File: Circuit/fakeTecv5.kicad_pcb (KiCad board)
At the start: 2 copper layers, 25.4 x 52.1 mm, 78 parts, among them J1 EXTRA, J11 FET1 3,3, J12 FET2 3,3, J13 FET3 3,3, J14 GPS Pins, J16 Encoder Pads, J37 SCL, J38 JST-SH-4, J39 SDA, J40 3.3V, J41 GND, J42 FET1, J43 FET2, J44 FET3, J45 GND, J46 3.3V, J47 GND, J48 GND, J49 GND, J5 I2C Oled screen, J50 3.3V, J51 GND, J52 GND, J6 FET1 Drain, J7 FET2 Drain, J8 FET3 Drain, J9 JST-PH-2, Q1 AO3400A, Q2 AO3400A, Q3 AO3400A, SW1 Reset, SW2 SW_Push, U1 XB8089D0, U2 HT-RA62, U3 nice!nano v2

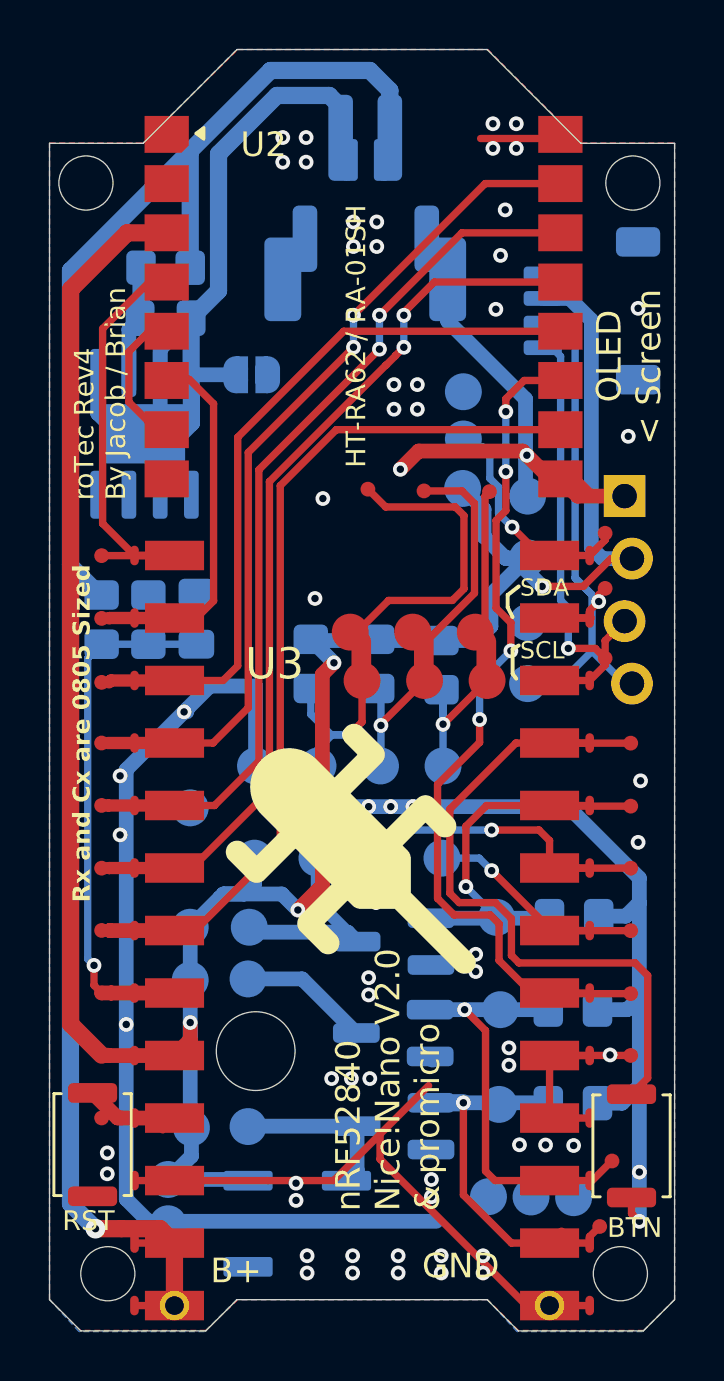
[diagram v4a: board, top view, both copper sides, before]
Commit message: hw: Battery connector clarification
Heltec LoRa32 is using Molex Picoblade... not JST
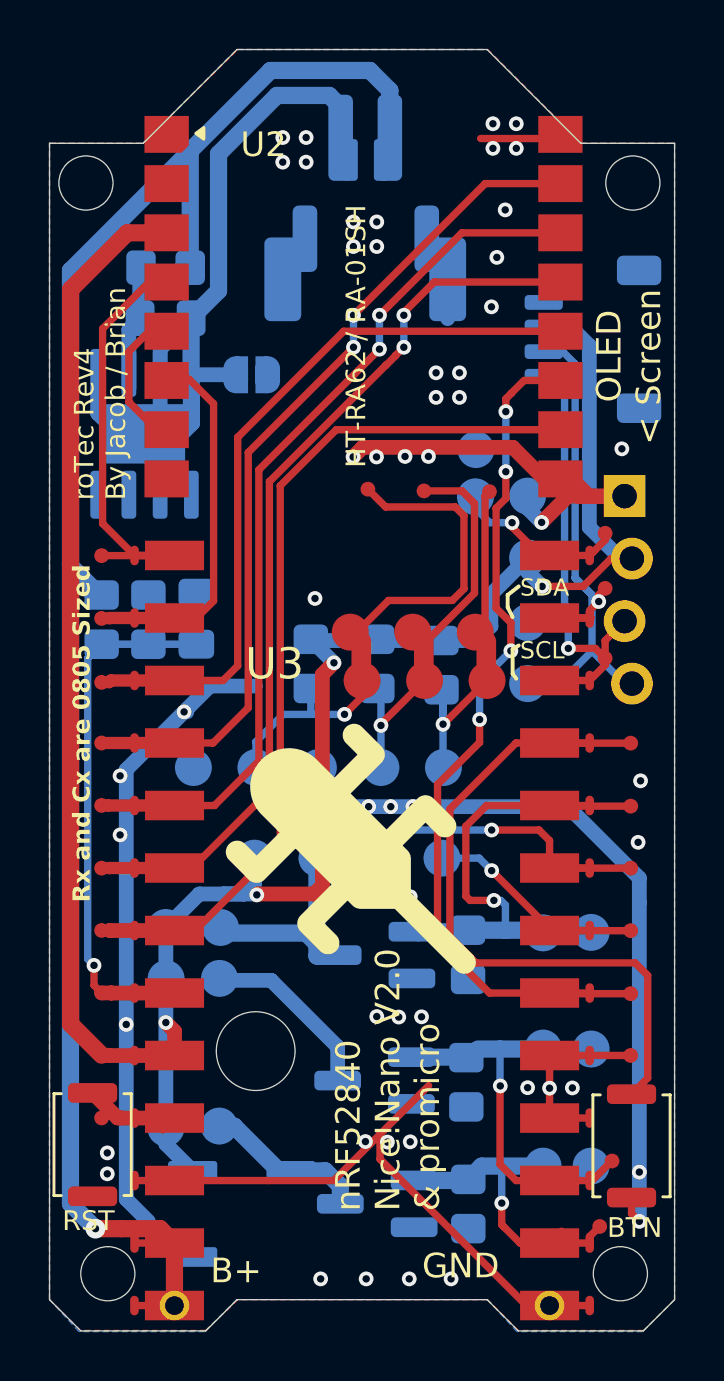
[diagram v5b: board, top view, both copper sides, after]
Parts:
- removed J46, J50: 3.3V, faketec:SMD_PAD_1x01
- removed J51, J52: GND, faketec:SMD_PAD_1x01
- J16: footprint faketec:SMD_PAD_1x04 -> faketec:SMD_PAD_1x05
- J9: value JST-PH-2 -> Molex PicoBlade 0532610271
- moved J49 10.8 mm to (120.9, 62.9)
- moved J48 7.31 mm to (120.9, 67.6)
- moved R3 5.90 mm to (115.9, 73.9), turned to 90 degrees
- moved R2 5.24 mm to (115.8, 69.0), turned to 90 degrees
- moved R1 4.59 mm to (115.9, 63.8), turned to 90 degrees
- moved Q3 3.23 mm to (112.2, 73.9)
- moved J44 3.08 mm to (118.9, 72.4)
- moved J47 2.74 mm to (120.9, 72.4)
- moved J16 2.52 mm to (104.7, 56.2)
- moved J45 2.40 mm to (116.2, 43.2)
- moved J1 2.40 mm to (116.2, 45.2)
- moved J43 2.34 mm to (118.9, 67.6)
- moved BZ1 2.29 mm to (106.7, 74.3)
- moved Q2 2.07 mm to (112.1, 68.9)
- moved J42 1.99 mm to (118.9, 62.9)
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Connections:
- J16 pad 3: /ENC_B -> GND
- J16 pad 4: /ENC_A -> /ENC_B
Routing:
- net GND: track 133.1 -> 108.4 mm, vias 67 -> 56
- net +3.3V: track 111.6 -> 100.8 mm
- net /FET3: track 16.3 -> 12.2 mm
- net /FET2: track 15.6 -> 12.5 mm
- net /EXTRA: track 7.40 -> 5.24 mm
- net /FET1: track 16.1 -> 18.1 mm
- net /GPS_GND: track 8.61 -> 10.6 mm
- net /VIBRATION: track 5.31 -> 7.30 mm
- net /SCL: track 19.4 -> 18.0 mm
- net /SDA: track 25.3 -> 24.1 mm
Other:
- board text added: "(EC11)"
- board text added: "5020 Buzzer >"
- board text added: "Direct GPIO Access"
- board text added: "P0.06( 6)"
- board text added: "P0.08( 8)"
- board text added: "P0.24(24)"
- board text added: "Qwiic"
- board text removed: "5020> Buzzer"
- board text removed: "<GND"
- board text removed: "P0.06 ( 6)"
- board text removed: "P0.08 ( 8)"
- board text removed: "P0.24 (24)"

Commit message: hw: Update schematic and connector to clarify battery connector
Including some photos and directions on locating the correct parts
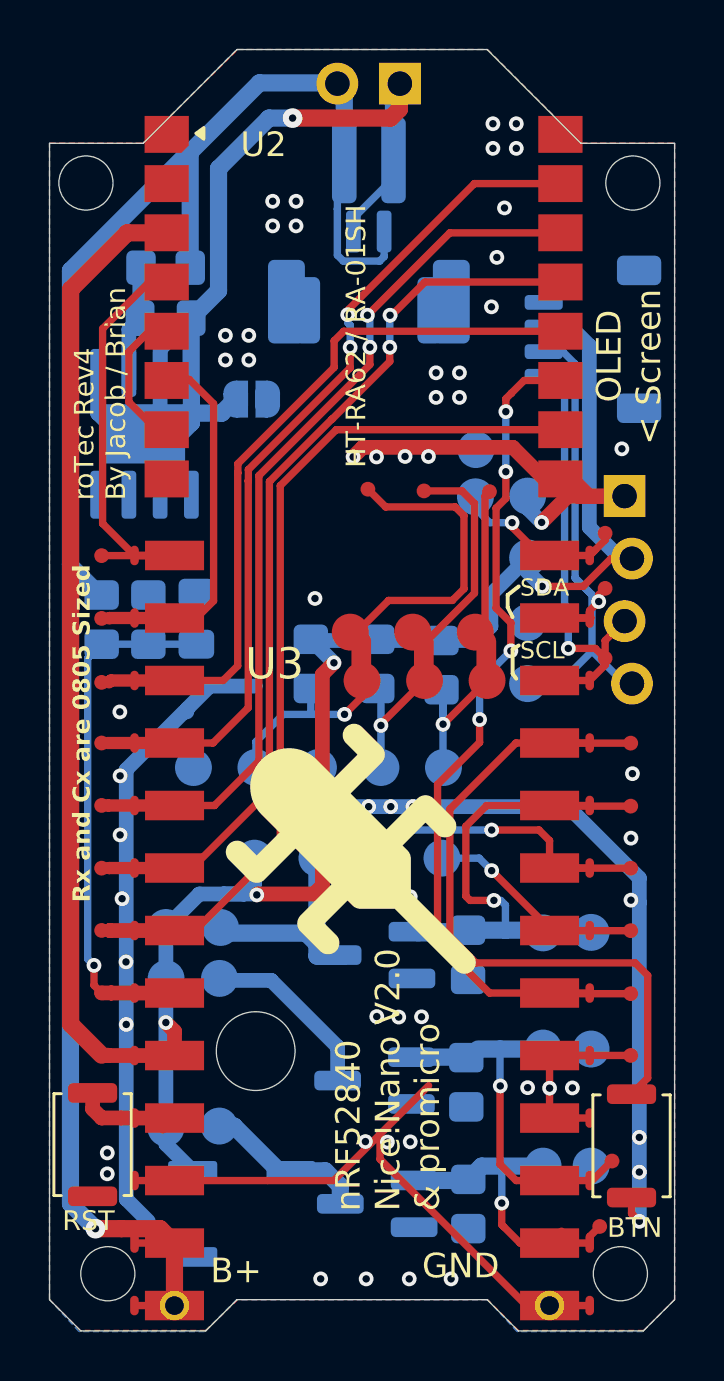
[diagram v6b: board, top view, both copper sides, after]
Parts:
- added J46: Conn_01x02_Socket, faketec:wirebond battery header, F.Cu at (113.1, 28.4)
- J9: footprint faketec:JST_PH_S2B-PH-SM4-TB_1x02-1MP_P2.00mm_Horizontal -> faketec:Combined_Battery_Connector_Molex_PicoBlade_P1.00_And_JST_PH_2.00mm
- moved JP1 0.99 mm to (107.1, 41.2)
- moved J9 0.92 mm to (111.9, 34.3)
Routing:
- net -BATT: track 32.9 -> 41.5 mm, vias 0 -> 1
- net GND: track 108.4 -> 103.7 mm, vias 56 -> 60
- net +BATT: track 72.7 -> 76.8 mm

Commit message: hw: Text Variable. Also mark as Rev5.
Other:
- board text added: "roTec Rev${REVISION} By Jacob / Brian"
- board text removed: "roTec Rev4 By Jacob / Brian"
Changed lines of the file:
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@@
 		)
 	)
+	(property "REVISION" "5")
 	(net 0 "")
 	(net 1 "/Batt%")
@@
 		(sheetname "/")
 		(sheetfile "fakeTecv5.kicad_sch")
-		(attr smd)
+		(attr smd exclude_from_bom)
 		(fp_text user "${REFERENCE}"
 			(at 0 -2.5 180)
@@
 			)
 		)
-		(property "Datasheet" "https://www.jst-mfg.com/product/pdf/eng/ePH.pdf"
+		(property "Datasheet" "https://www.molex.com/content/dam/molex/molex-dot-com/products/automated/en-us/salesdrawingpdf/532/53261/532610271_sd.pdf?inline"
 			(at 0 0 0)
 			(layer "B.Fab")
@@
 			)
 		)
-		(property "Description" "Combined footprint for JST_PH_S2B-PH-SM4-TB and JST_GH_SM02B-GHS-TB"
+		(property "Description" "1.25mm Pitch, PicoBlade PCB Header, Single Row, Right-Angle, Surface Mount, Tin (Sn) Plating, Friction Lock, 2 Circuits, Natural, Tape and Reel"
 			(at 0 0 0)
 			(layer "B.Fab")
@@
 		(layer "B.Mask")
 	)
-	(gr_line
-		(start 117.7 51.35)
-		(end 117.7 52.35)
-		(stroke
-			(width 0.16)
-			(type default)
-		)
-		(layer "F.SilkS")
-	)
-	(gr_line
-		(start 117.5 49.15)
-		(end 117.5 49.65)
-		(stroke
-			(width 0.16)
-			(type default)
-		)
-		(layer "F.SilkS")
-	)
 	(gr_poly
 		(pts
@@
 	)
 	(gr_line
-		(start 117.7 52.35)
-		(end 117.85 52.55)
-		(stroke
-			(width 0.16)
-			(type default)
-		)
-		(layer "F.SilkS")
-	)
-	(gr_line
-		(start 117.5 49.65)
-		(end 117.7 50.05)
-		(stroke
-			(width 0.16)
-			(type default)
-		)
-		(layer "F.SilkS")
-	)
-	(gr_line
-		(start 117.7 51.35)
-		(end 117.95 51.2)
-		(stroke
-			(width 0.16)
-			(type default)
-		)
-		(layer "F.SilkS")
-	)
-	(gr_line
-		(start 117.95 48.8)
-		(end 117.5 49.15)
-		(stroke
-			(width 0.16)
-			(type default)
-		)
-		(layer "F.SilkS")
-	)
-	(gr_line
 		(start 118.81 60.89)
 		(end 118.81 61.43)
@@
 		)
 	)
-	(gr_text "SDA"
-		(at 118 48.85 0)
-		(layer "F.SilkS")
-		(effects
-			(font
-				(size 0.7 0.7)
-				(thickness 0.16)
-			)
-			(justify left)
-		)
-	)
 	(gr_text "nRF52840\nNice!Nano V2.0\n& promicro"
 		(at 114.83 74.19 90)
@@
 		)
 	)
-	(gr_text "roTec Rev4\nBy Jacob / Brian"
+	(gr_text "roTec Rev${REVISION}\nBy Jacob / Brian"
 		(at 102.05 45.3 90)
 		(layer "F.SilkS" knockout)
@@
 		)
 	)
-	(gr_text "SCL"
-		(at 118 51.4 0)
-		(layer "F.SilkS")
-		(effects
-			(font
-				(size 0.7 0.7)
-				(thickness 0.16)
-			)
-			(justify left)
-		)
-	)

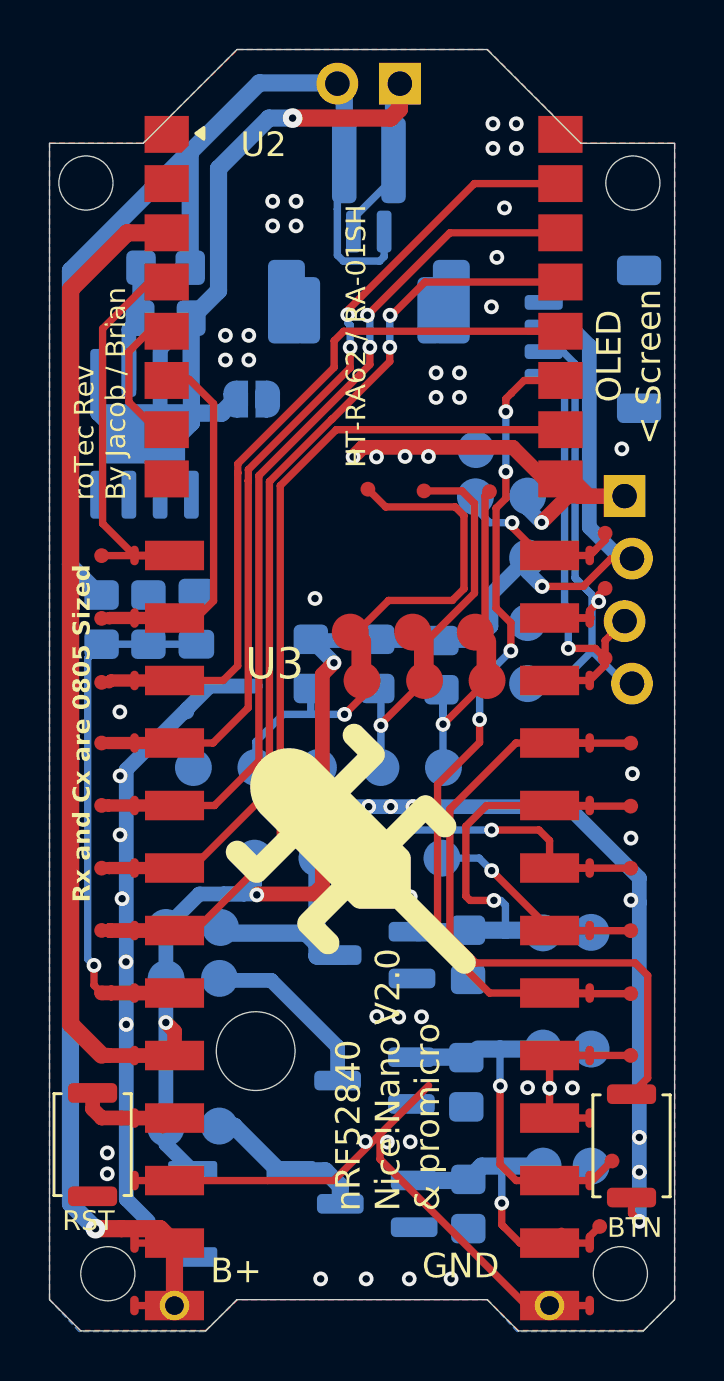
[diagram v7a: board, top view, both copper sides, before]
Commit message: hw: Add JST-SH-4 for encoder. Marked as Rev5.1
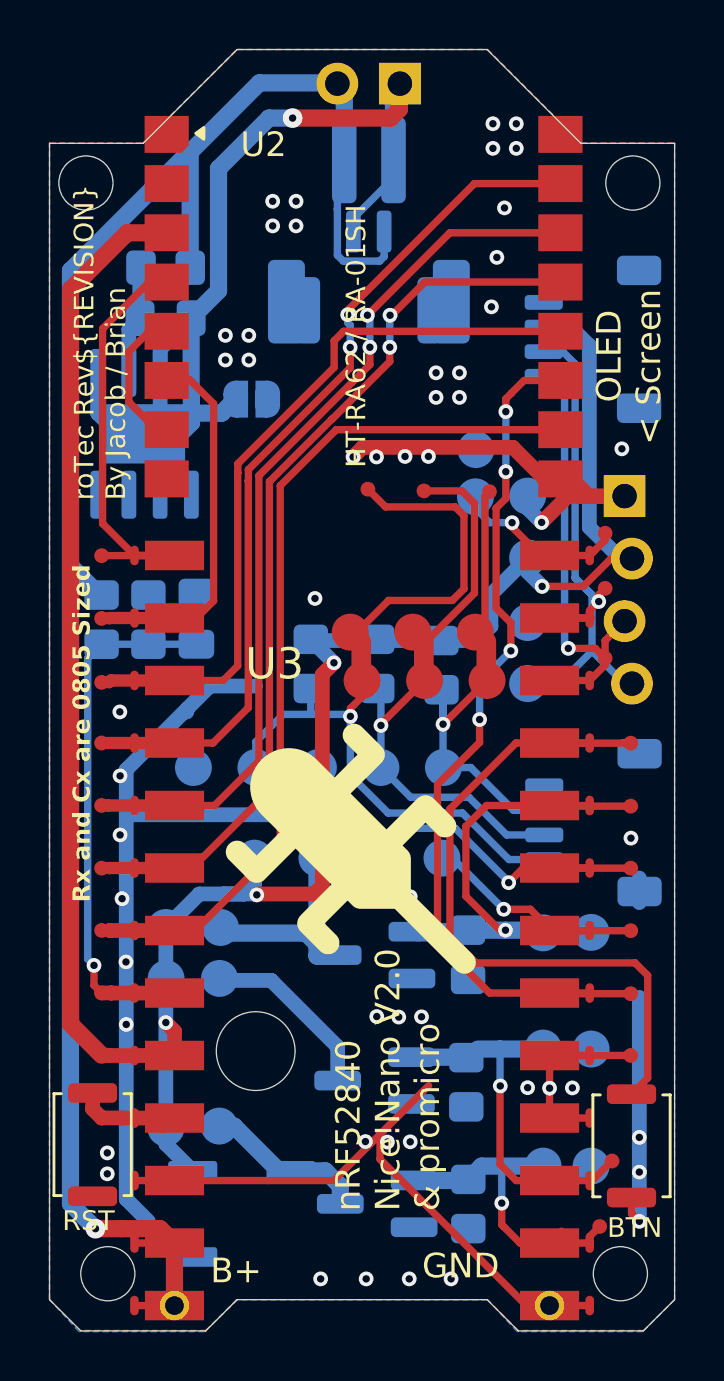
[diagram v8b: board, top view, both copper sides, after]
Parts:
- added J50: JST-SH-4, Connector_JST:JST_SH_SM04B-SRSS-TB_1x04-1MP_P1.00mm_Horizontal, B.Cu at (121.0, 58.4)
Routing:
- net /ENC_PUSH: track 21.1 -> 33.2 mm
- net GND: track 103.7 -> 93.8 mm, vias 60 -> 55
- net /ENC_B: track 15.1 -> 22.9 mm
- net /ENC_A: track 13.4 -> 18.2 mm
- net /FET1: track 18.1 -> 17.5 mm
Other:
- board text added: "ENC"
- board text added: "JST-SH-4"
- board text added: "SEL"
- board text removed: "Direct GPIO Access"
- board text removed: "Qx: N-CHN MOSFET AO3400A"
